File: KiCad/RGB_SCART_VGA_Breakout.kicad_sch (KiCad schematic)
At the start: 22 parts, among them J1 SCART-F, J11 SJ1-3535NG, J2 Mini-DIN-4, J3 DE15_Plug_HighDensity_Mountin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, J4 Conn_01x09, J5 Mounting, J6 Mounting, J7 Mounting, J8 Mounting

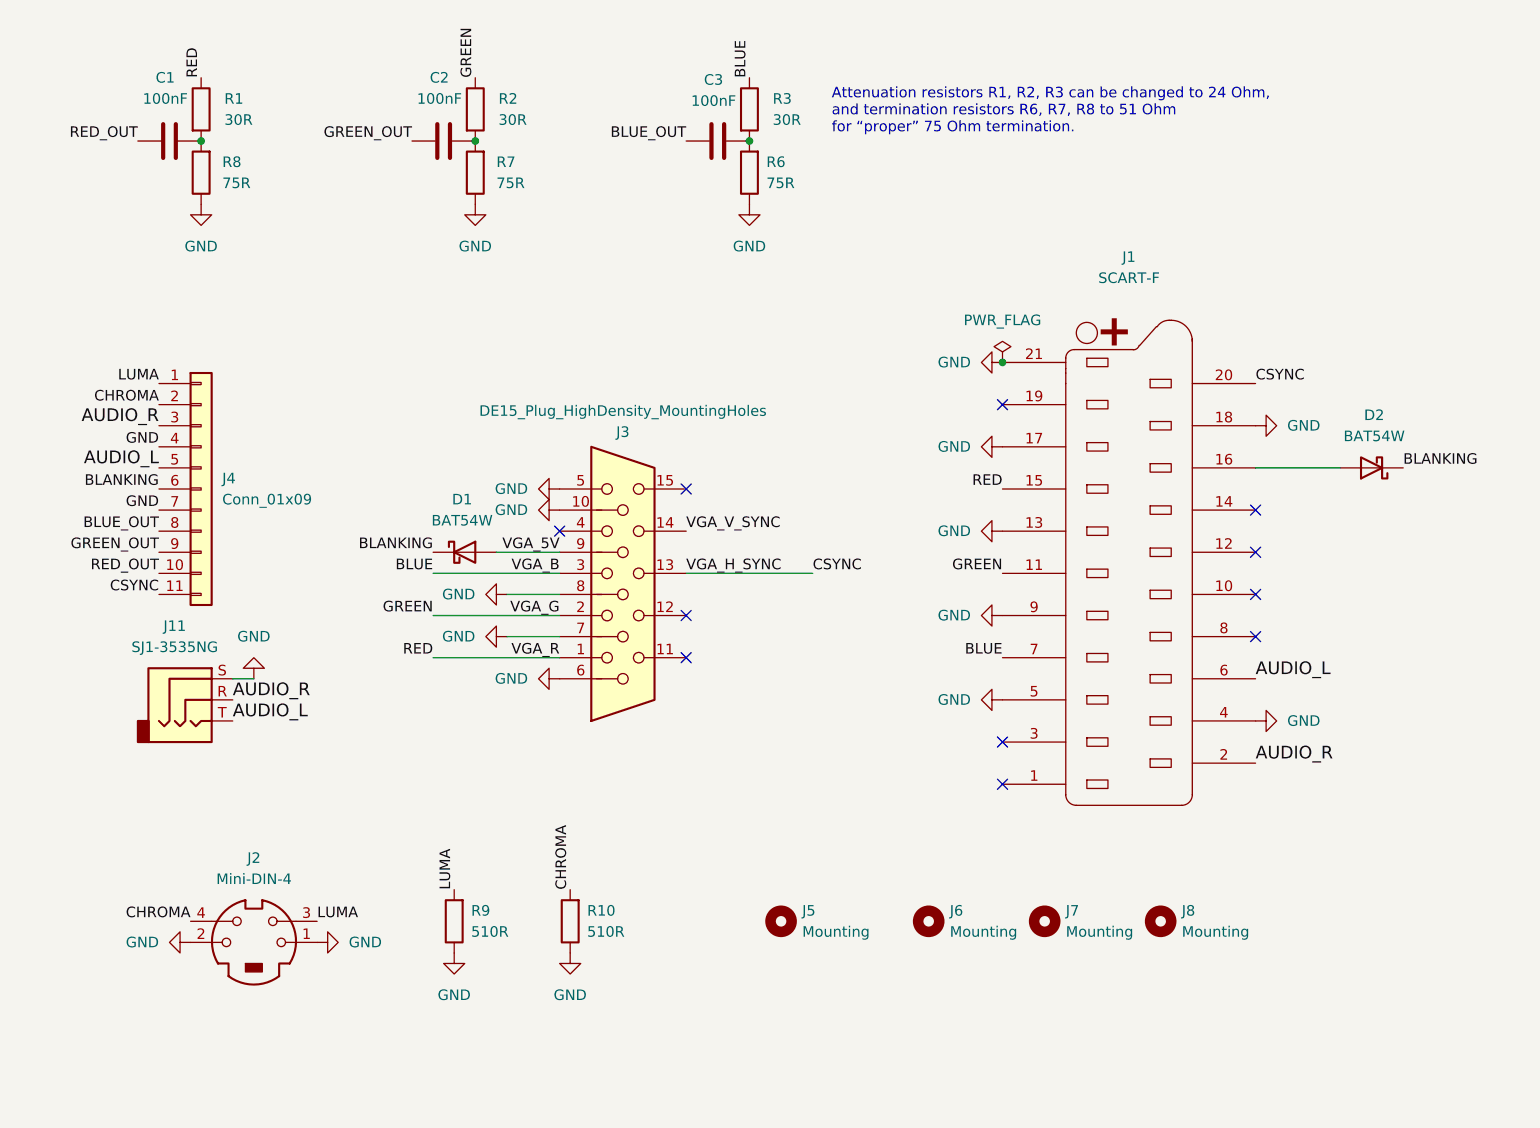
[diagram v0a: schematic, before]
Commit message: Added blanking voltage divider / pulldown resistors with description. Expanded RGB load / voltage divider resistors description.
PCB version 1.1.
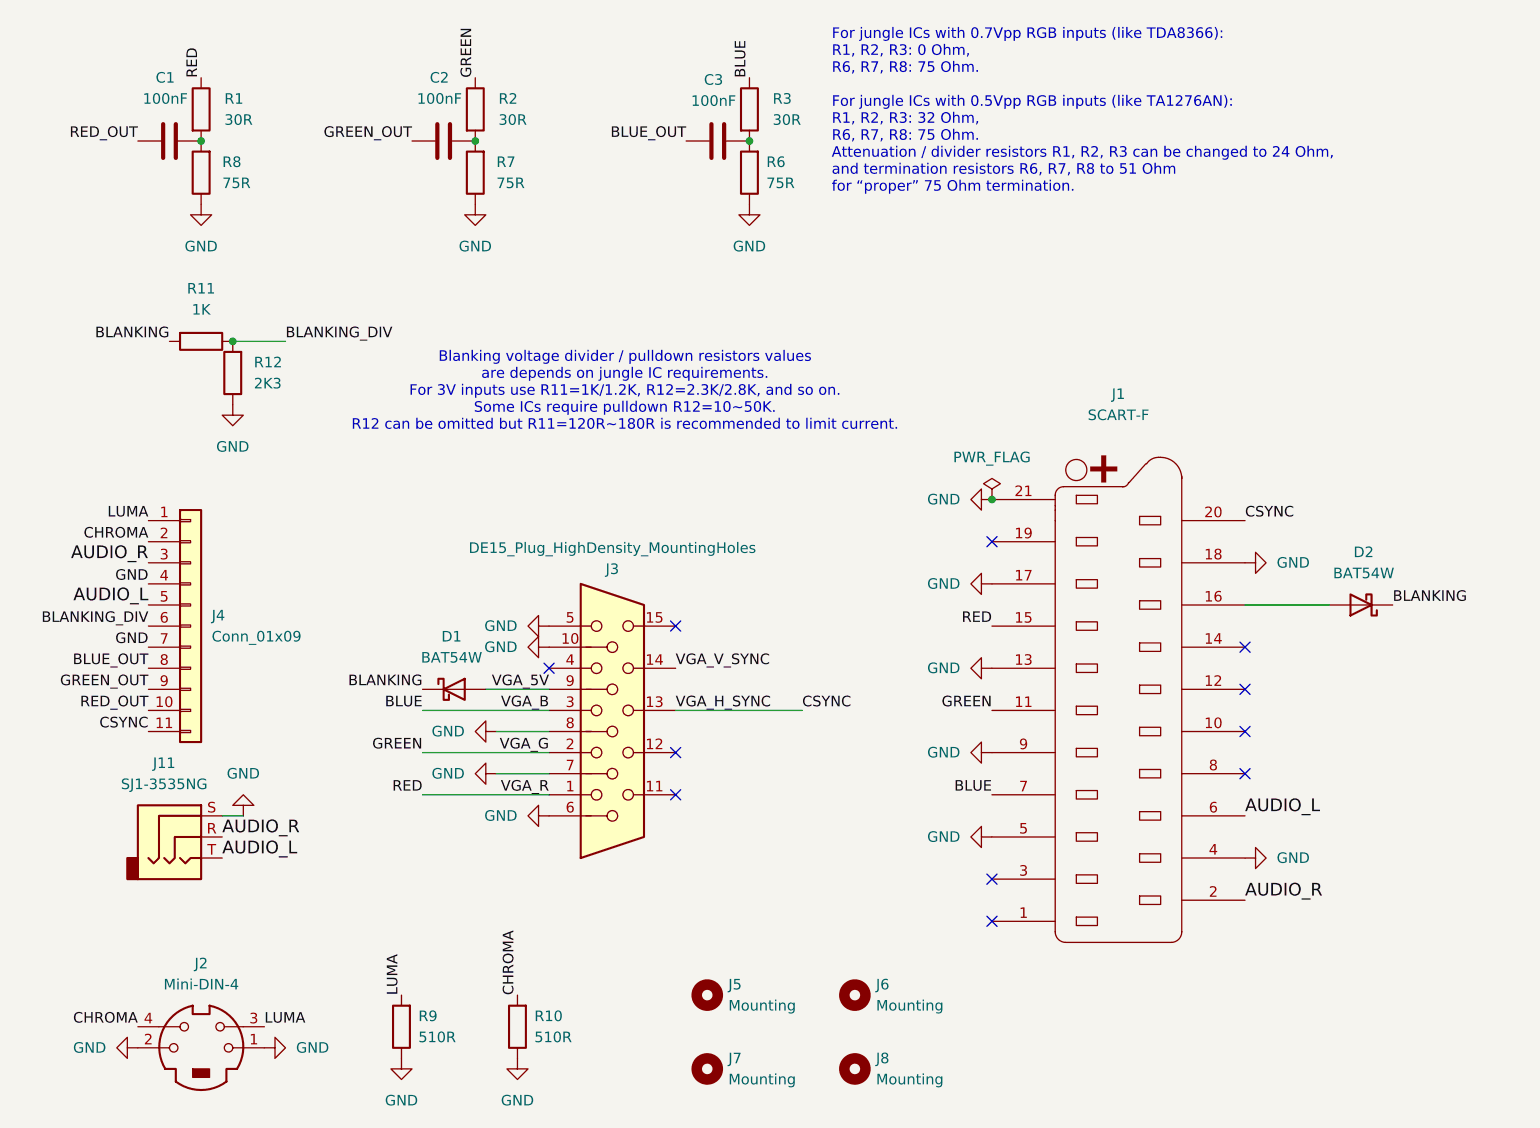
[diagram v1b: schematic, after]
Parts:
- added R11: 1K, Resistor_SMD:R_0805_2012Metric, symbol Device:R
- added R12: 2K3, Resistor_SMD:R_0805_2012Metric, symbol Device:R
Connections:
- net BLANKING: now also R11.2; no longer J4.6 (Pin_6)
- net GND: now also R12.1
- new net BLANKING_DIV: J4.6 (Pin_6), R11.1, R12.2
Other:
- note added: "Blanking voltage divider / pulldown resistors values are depends on jungle IC requirements. For 3V inputs use R11=1K/1.2K, R12=2.3K/2.8K, and so on. Some ICs require pulldown R12=10~50K. R12 can be omitted but R11=120R~180R is recommended to limit current."
- note added: "For jungle ICs with 0.7Vpp RGB inputs (like TDA8366): R1, R2, R3: 0 Ohm, R6, R7, R8: 75 Ohm. For jungle ICs with 0.5Vpp RGB inputs (like TA1276AN): R1, R2, R3: 32 Ohm, R6, R7, R8: 75 Ohm. Attenuation / divider resistors R1, R2, R3 can be changed to 24 Ohm, and termination resistors R6, R7, R8 to 51 Ohm for “proper” 75 Ohm termination."
- note removed: "Attenuation resistors R1, R2, R3 can be changed to 24 Ohm, and termination resistors R6, R7, R8 to 51 Ohm for “proper” 75 Ohm termination."
- moved on the sheet: D1, D2, J1, J11, J2, J3, J4, J5, J6, J7, J8, R10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
